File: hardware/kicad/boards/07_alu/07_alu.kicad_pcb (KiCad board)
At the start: 2 copper layers, 99.8 x 99.7 mm, 185 parts, among them J10 Conn_01x04_Pin, J11 Conn_01x04_Pin, J12 Conn_01x08_Pin, J15 Conn_01x08_Pin, J16 Conn_01x08_Pin, J17 Conn_01x08_Pin, J5 Conn_01x08_Pin, J6 Conn_01x08_Pin, J7 Conn_01x08_Pin, U16 74ACT151, U3 74ACT283, U36 74HC86, U37 74LS08, U38 74LS540, U4 74HC688, U40 74LS377, U41 74ACT151, U42 74ACT151, U43 74ACT151, U44 74ACT151, U45 74ACT151, U46 74ACT151, U47 74ACT151, U48 74ACT151, U49 74ACT151, U5 74ACT283, U50 74ACT151, U51 74ACT151, U52 74ACT151, U53 74ACT151, U54 74ACT151, U55 74ACT151, U56 74ACT151

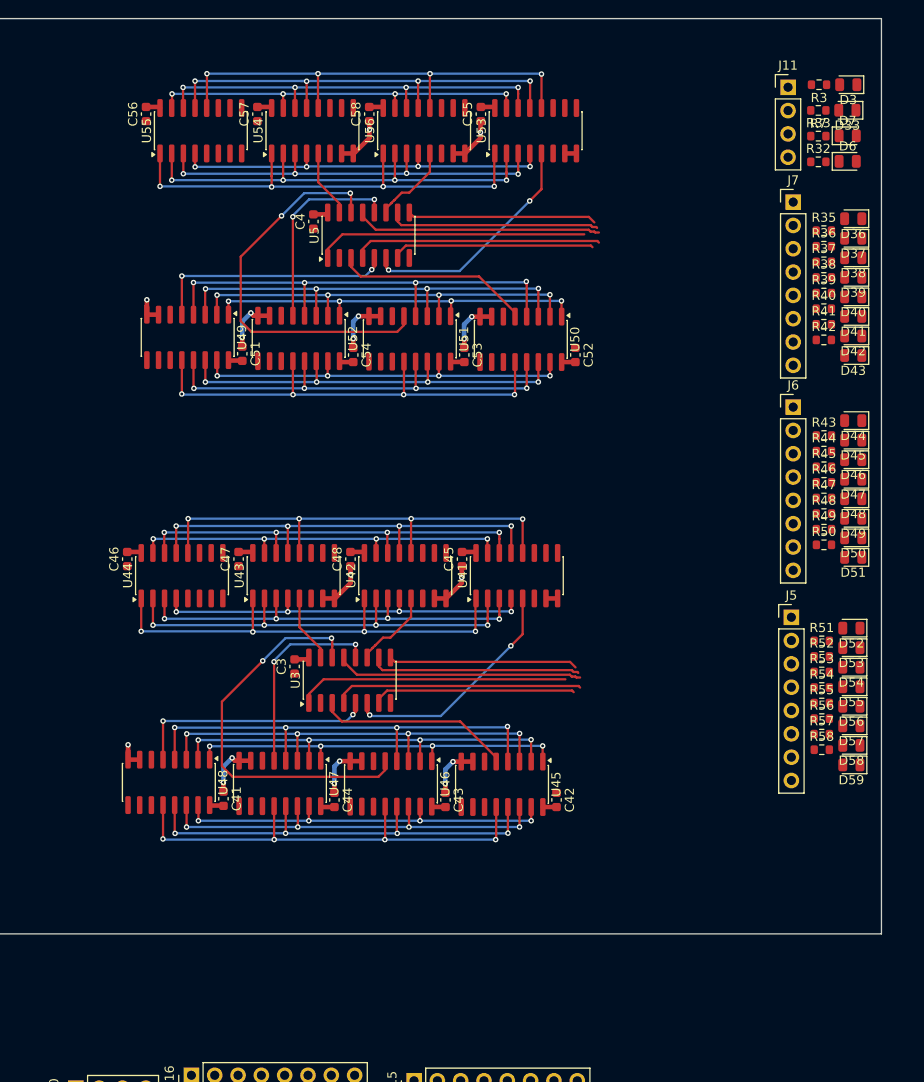
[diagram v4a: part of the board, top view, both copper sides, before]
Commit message: feat: routed 4b cells; placing resistor network components
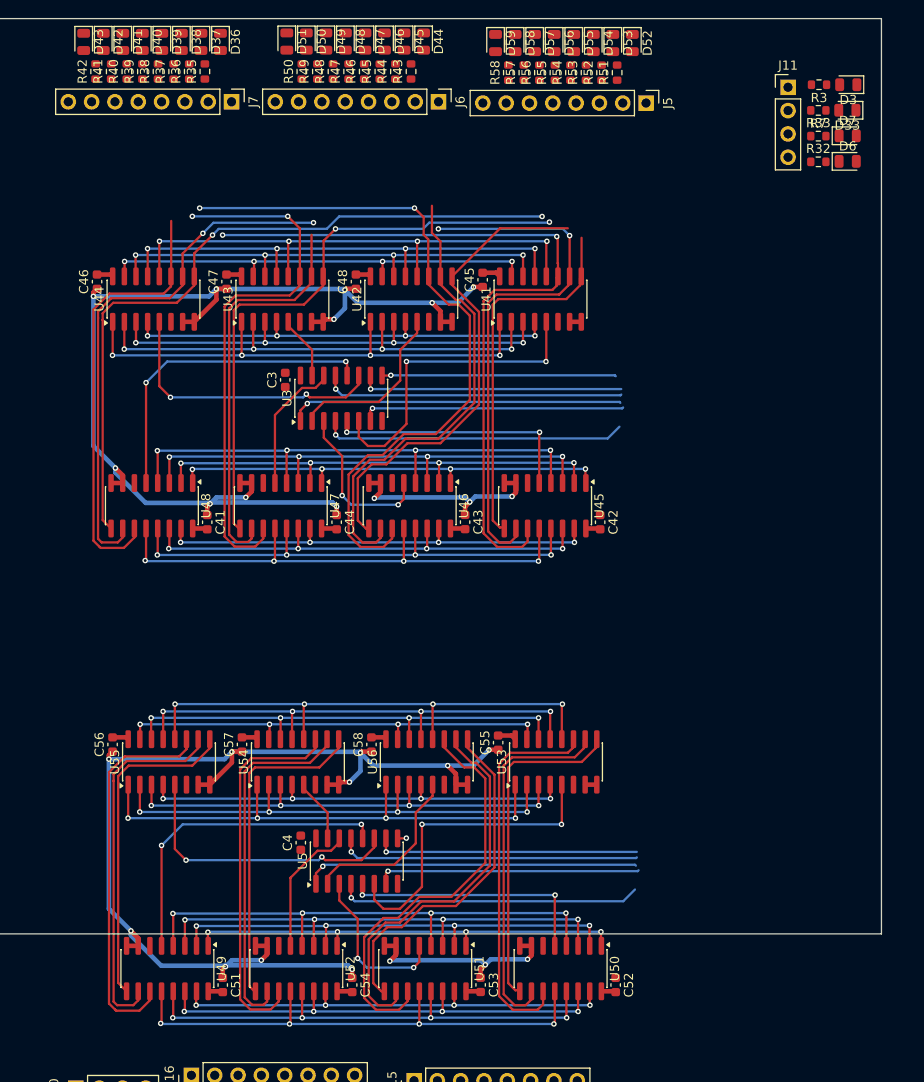
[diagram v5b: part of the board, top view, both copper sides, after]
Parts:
- moved D43 90.5 mm to (69.3, 45.8), turned to -90 degrees
- moved D42 87.7 mm to (71.4, 45.8), turned to -90 degrees
- moved D59 87.7 mm to (114.2, 46.0), turned to -90 degrees
- moved D41 85.0 mm to (73.6, 45.8), turned to -90 degrees
- moved D58 84.8 mm to (116.3, 46.0), turned to -90 degrees
- moved R42 84.5 mm to (70.6, 49.1), turned to 90 degrees
- moved D51 83.4 mm to (91.4, 45.8), turned to -90 degrees
- moved R41 82.4 mm to (72.3, 49.1), turned to 90 degrees
- moved D40 82.3 mm to (75.7, 45.8), turned to -90 degrees
- moved D57 82.0 mm to (118.4, 46.0), turned to -90 degrees
- moved R58 81.3 mm to (115.6, 49.2), turned to 90 degrees
- moved D50 80.4 mm to (93.6, 45.8), turned to -90 degrees
- moved R40 80.2 mm to (74.0, 49.1), turned to 90 degrees
- moved D39 79.6 mm to (77.8, 45.8), turned to -90 degrees
- moved D56 79.2 mm to (120.6, 46.0), turned to -90 degrees
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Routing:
- net GND: track 67.1 -> 293.0 mm, vias 18 -> 26
- net A0: track 0.00 -> 83.2 mm, vias 0 -> 2
- net C3: track 0.00 -> 78.2 mm, vias 0 -> 2
- net A1: track 0.00 -> 77.4 mm, vias 0 -> 2
- net C2: track 0.00 -> 65.6 mm, vias 0 -> 2
- net B0: track 0.00 -> 59.4 mm, vias 0 -> 2
- net A2: track 0.00 -> 59.1 mm, vias 0 -> 2
- net B3: track 0.00 -> 58.8 mm, vias 0 -> 2
- net C1: track 0.00 -> 52.6 mm
- net B1: track 0.00 -> 51.0 mm
- net A3: track 0.00 -> 48.0 mm
- net A5: track 0.00 -> 45.9 mm
- net B2: track 0.00 -> 43.9 mm
- net B5: track 0.00 -> 42.9 mm
- net A4: track 0.00 -> 42.2 mm
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
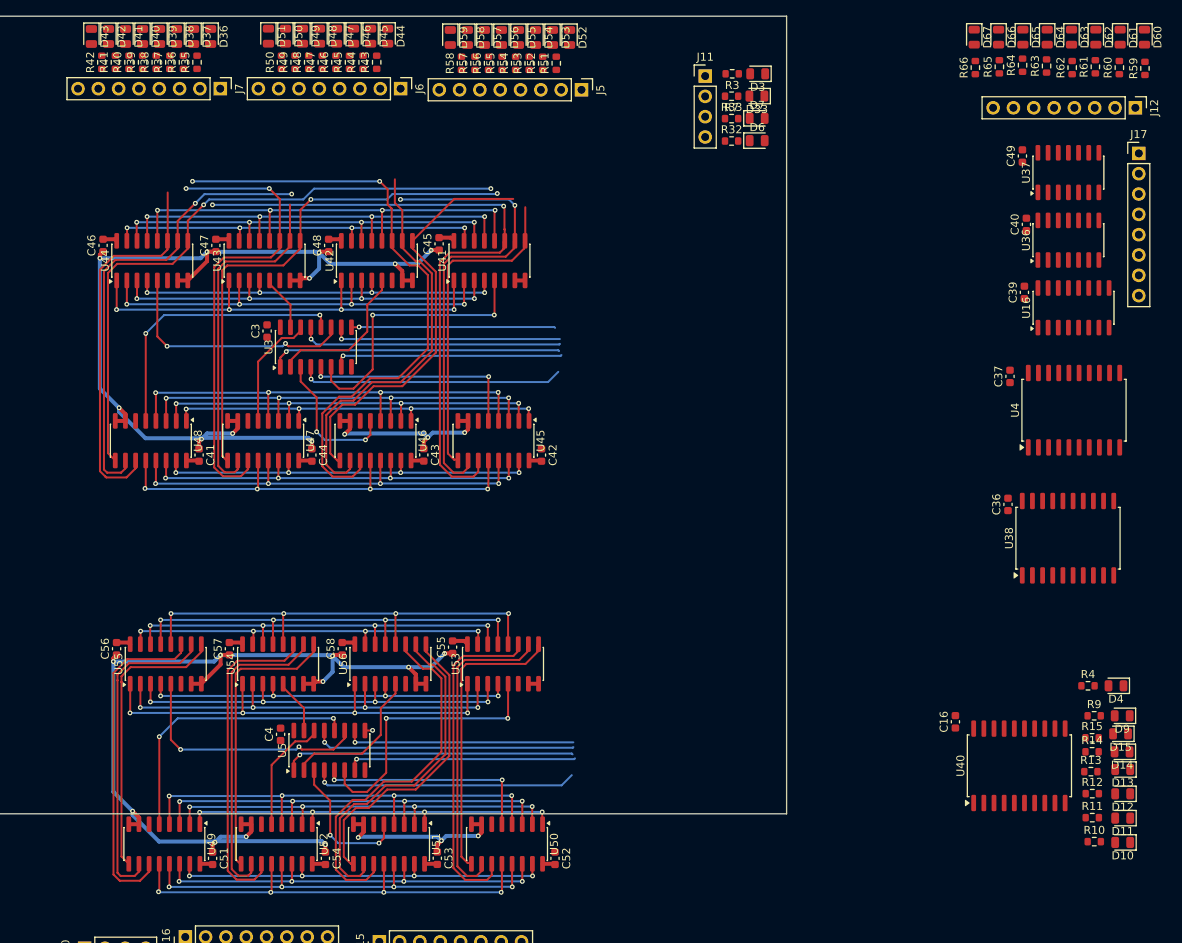
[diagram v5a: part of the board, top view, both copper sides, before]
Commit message: checkpoint: routed all 16b cells; pending output routing
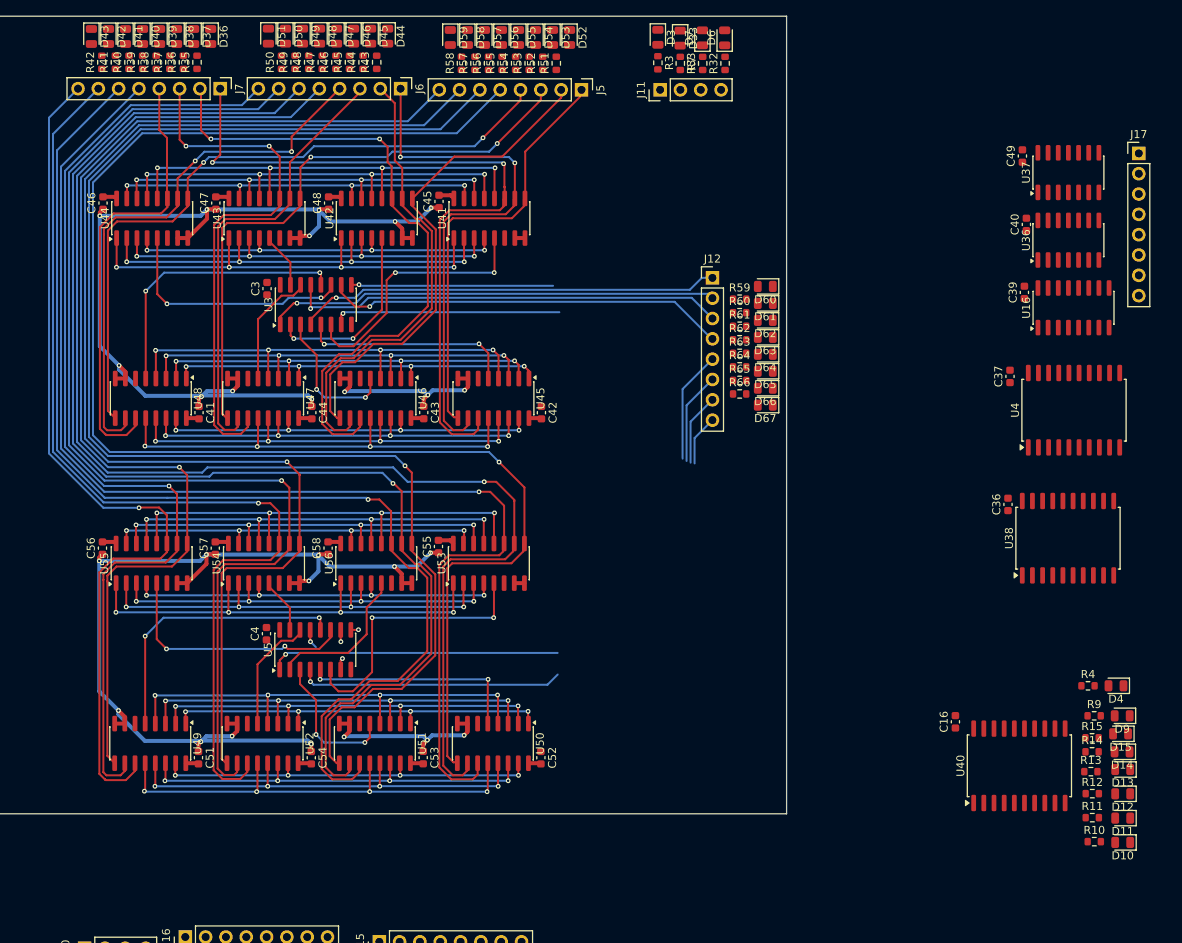
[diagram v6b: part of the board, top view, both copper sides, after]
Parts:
- moved R59 58.3 mm to (150.3, 78.7), turned to 0 degrees
- moved J12 57.0 mm to (146.9, 76.0), turned to 0 degrees
- moved D60 56.7 mm to (153.5, 77.1), turned to 180 degrees
- moved R60 56.5 mm to (150.3, 80.4), turned to 0 degrees
- moved D61 55.5 mm to (153.5, 79.2), turned to 180 degrees
- moved R61 55.0 mm to (150.3, 82.1), turned to 0 degrees
- moved D62 54.4 mm to (153.5, 81.3), turned to 180 degrees
- moved R62 53.7 mm to (150.3, 83.7), turned to 0 degrees
- moved D63 53.6 mm to (153.5, 83.4), turned to 180 degrees
- moved D64 53.0 mm to (153.5, 85.6), turned to 180 degrees
- moved D67 52.9 mm to (153.5, 91.9), turned to 180 degrees
- moved D65 52.7 mm to (153.5, 87.7), turned to 180 degrees
- moved D66 52.7 mm to (153.5, 89.8), turned to 180 degrees
- moved R63 52.6 mm to (150.3, 85.4), turned to 0 degrees
- moved R64 51.7 mm to (150.3, 87.1), turned to 0 degrees
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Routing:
- net C4: track 36.5 -> 187.5 mm, vias 0 -> 1
- net C5: track 37.9 -> 174.5 mm, vias 0 -> 1
- net B4: track 40.2 -> 172.0 mm, vias 0 -> 1
- net C6: track 36.0 -> 157.3 mm, vias 0 -> 1
- net B5: track 42.9 -> 159.7 mm, vias 0 -> 1
- net A4: track 42.2 -> 154.3 mm, vias 0 -> 1
- net C7: track 36.0 -> 141.8 mm, vias 0 -> 1
- net B6: track 39.4 -> 140.8 mm, vias 0 -> 1
- net A5: track 45.9 -> 143.2 mm, vias 0 -> 1
- net B7: track 40.2 -> 125.7 mm, vias 0 -> 1
- net A6: track 41.2 -> 124.3 mm, vias 0 -> 1
- net A7: track 42.0 -> 110.7 mm, vias 0 -> 1
- net /alu_4b_0/cout: track 54.3 -> 26.7 mm
- net OUT2: track 32.9 -> 54.8 mm
- net OUT3: track 28.8 -> 50.3 mm
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
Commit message: checkpoint: routed output and opcode buses
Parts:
- moved D32 113.5 mm to (153.4, 58.0), turned to 180 degrees
- moved D31 112.2 mm to (153.4, 60.2), turned to 180 degrees
- moved D30 110.9 mm to (153.4, 62.3), turned to 180 degrees
- moved D29 109.8 mm to (153.4, 64.4), turned to 180 degrees
- moved D28 108.8 mm to (153.4, 66.6), turned to 180 degrees
- moved R31 108.2 mm to (150.2, 59.4), turned to 0 degrees
- moved D27 107.8 mm to (153.4, 68.7), turned to 180 degrees
- moved R30 107.3 mm to (150.2, 61.1), turned to 0 degrees
- moved D26 107.0 mm to (153.4, 70.8), turned to 180 degrees
- moved R29 106.4 mm to (150.2, 62.8), turned to 0 degrees
- moved D25 106.2 mm to (153.4, 72.9), turned to 180 degrees
- moved R28 105.6 mm to (150.2, 64.5), turned to 0 degrees
- moved R27 104.9 mm to (150.2, 66.2), turned to 0 degrees
- moved R26 104.3 mm to (150.2, 67.9), turned to 0 degrees
- moved R25 103.8 mm to (150.2, 69.6), turned to 0 degrees
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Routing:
- net OUT6: track 11.4 -> 57.0 mm
- net OUT7: track 7.82 -> 50.8 mm
- net ALU_OPCODE_Y4: track 97.6 -> 133.1 mm
- net ALU_OPCODE_Y5: track 103.1 -> 136.5 mm
- net ALU_OPCODE_Y6: track 108.7 -> 139.8 mm
- net ALU_OPCODE_X0: track 113.9 -> 144.0 mm
- net ALU_OPCODE_Y7: track 115.2 -> 144.9 mm
- net ALU_OPCODE_X7: track 114.3 -> 142.7 mm
- net ALU_OPCODE_X1: track 108.4 -> 136.4 mm
- net ALU_OPCODE_X6: track 109.0 -> 136.8 mm
- net ALU_OPCODE_X5: track 103.5 -> 130.8 mm
- net ALU_OPCODE_X2: track 103.1 -> 130.2 mm
- net CIN-MAIN: track 28.6 -> 1.69 mm
- net ALU_OPCODE_X4: track 98.0 -> 124.9 mm
- net ALU_OPCODE_X3: track 97.6 -> 124.5 mm
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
